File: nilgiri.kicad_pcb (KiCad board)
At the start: 2 copper layers, 130 x 72 mm, 32 parts, among them SW1 SW_PUSH, SW10 SW_PUSH, SW11 SW_PUSH, SW12 SW_PUSH, SW13 SW_PUSH, SW2 SW_PUSH, SW3 SW_PUSH, SW4 SW_PUSH, SW5 SW_PUSH, SW6 SW_PUSH, SW7 SW_PUSH, SW8 SW_PUSH, SW9 SW_PUSH, U1 ProMicro

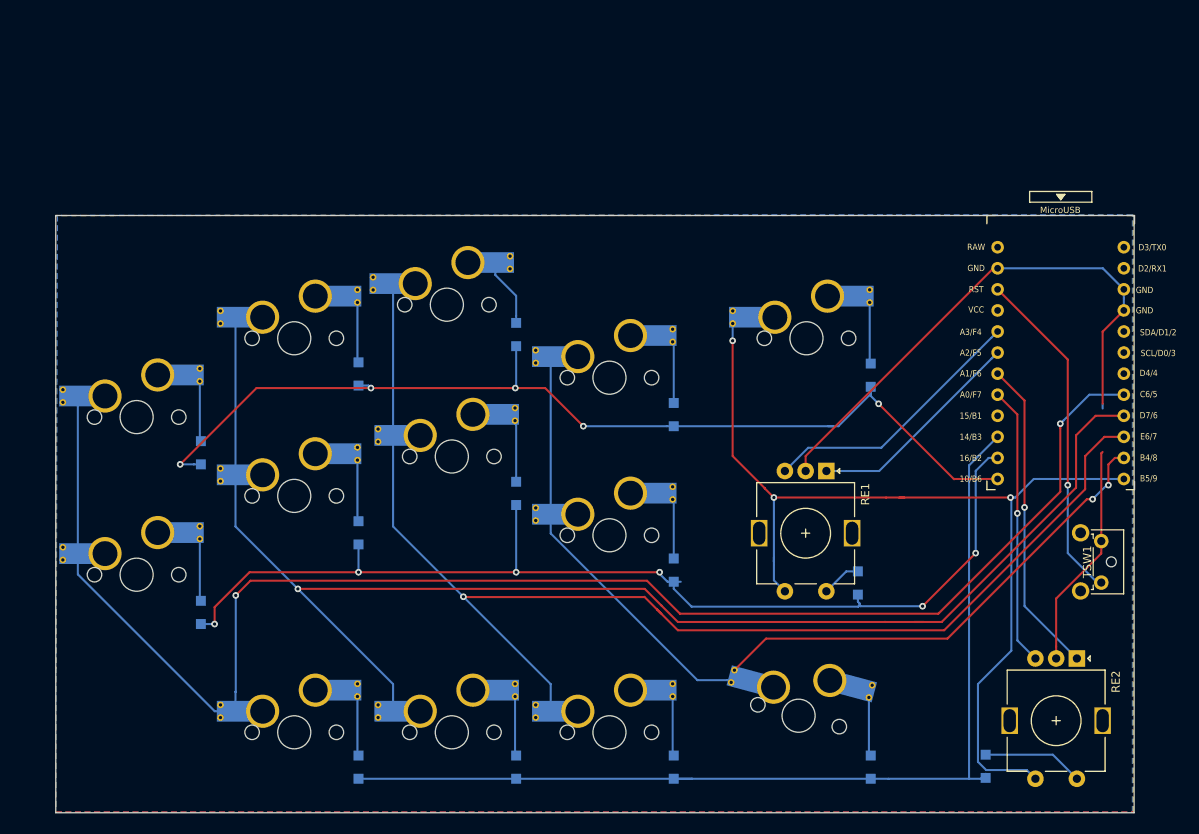
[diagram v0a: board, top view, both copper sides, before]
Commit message: merged onboard type / added footprints
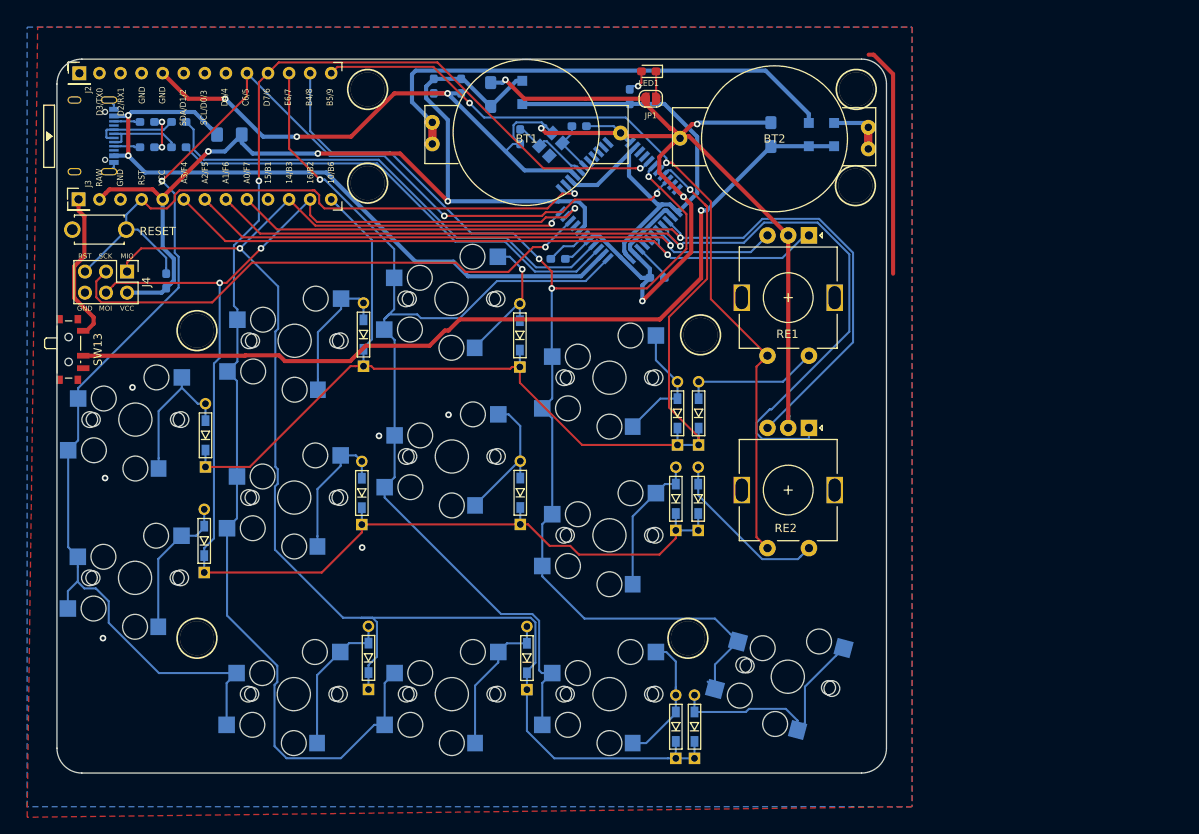
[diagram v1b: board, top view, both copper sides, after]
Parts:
- removed the D15 at (184.2, 76.2)
- removed D2: D, _keebio:D_SOD123F
- removed TSW1: SW_RESET, _keebio:SW_Tactile_SPST_Angled_MJTP1117
- added BT1: Battery_Cell, nilgiri:HU1632, F.Cu at (142.7, 47.0)
- added BT2: Battery_Cell, nilgiri:HU1632, F.Cu at (172.6, 47.8)
- added C1: 10u, Capacitor_Tantalum_SMD:CP_EIA-3216-10_Kemet-I_Pad1.58x1.35mm_HandSolder, B.Cu at (138.4, 42.4)
- added C2: 22p, Capacitor_SMD:C_0603_1608Metric_Pad1.05x0.95mm_HandSolder, B.Cu at (142.0, 47.5)
- added C3: 0.1u, Capacitor_SMD:C_0603_1608Metric_Pad1.05x0.95mm_HandSolder, B.Cu at (158.5, 64.5)
- added C5: 22p, Capacitor_SMD:C_0603_1608Metric_Pad1.05x0.95mm_HandSolder, B.Cu at (149.1, 46.2)
- added C6: 1u, Capacitor_SMD:C_0603_1608Metric_Pad1.05x0.95mm_HandSolder, B.Cu at (134.9, 41.4)
- added C7: 1u, Capacitor_SMD:C_0603_1608Metric_Pad1.05x0.95mm_HandSolder, B.Cu at (146.6, 62.2)
- added C8: 0.1u, Capacitor_SMD:C_0603_1608Metric_Pad1.05x0.95mm_HandSolder, B.Cu at (131.6, 41.4)
- added C9: 10u, Capacitor_Tantalum_SMD:CP_EIA-3216-10_Kemet-I_Pad1.58x1.35mm_HandSolder, B.Cu at (172.2, 47.2)
- added D21: 1N5819W, Keebio:D_SOD123F, B.Cu at (142.2, 42.2)
- added D31: 1N5819W, Keebio:D_SOD123F, B.Cu at (176.8, 47.2)
- added D32: 1N5819W, Keebio:D_SOD123F, B.Cu at (179.8, 47.2)
- added D5: 1N4148W, nilgiri:D3_TH_SMD, B.Cu at (103.9, 96.2)
- added F1: 500mA, Fuse:Fuse_1206_3216Metric_Pad1.42x1.75mm_HandSolder, B.Cu at (106.9, 47.2)
- added J1: USB-C, Connector_USB:USB_C_Receptacle_Palconn_UTC16-G, B.Cu at (90.5, 47.4)
- added J2: BAT-, Connector_PinHeader_2.54mm:PinHeader_1x01_P2.54mm_Vertical, F.Cu at (88.8, 39.9)
- added J3: BAT+, Connector_PinHeader_2.54mm:PinHeader_1x01_P2.54mm_Vertical, F.Cu at (88.8, 55.0)
- added J4: ISP, Connector_PinHeader_2.54mm:PinHeader_2x03_P2.54mm_Vertical, F.Cu at (94.6, 63.8)
- added JP1: LED_ENABLE, Jumper:SolderJumper-2_P1.3mm_Open_RoundedPad1.0x1.5mm, F.Cu at (157.7, 42.9)
- added LED1: PWR, LED_SMD:LED_0603_1608Metric_Pad1.05x0.95mm_HandSolder, F.Cu at (157.5, 39.6)
- added R1: 10k, Resistor_SMD:R_0603_1608Metric_Pad1.05x0.95mm_HandSolder, B.Cu at (99.3, 64.9)
- added R2: 1k, Resistor_SMD:R_0603_1608Metric_Pad1.05x0.95mm_HandSolder, B.Cu at (155.2, 42.7)
- added R3: 5.1k, Resistor_SMD:R_0603_1608Metric_Pad1.05x0.95mm_HandSolder, B.Cu at (97.0, 48.8)
- added R4: 5.1k, Resistor_SMD:R_0603_1608Metric_Pad1.05x0.95mm_HandSolder, B.Cu at (97.0, 45.7)
- added R5: 22, Resistor_SMD:R_0603_1608Metric_Pad1.05x0.95mm_HandSolder, B.Cu at (100.8, 48.8)
- added R6: 22, Resistor_SMD:R_0603_1608Metric_Pad1.05x0.95mm_HandSolder, B.Cu at (100.8, 45.7)
- added REF**: M2_spacer, nilgiri:M2_spacer, F.Cu at (162.2, 108.0)
- added REF**: M2_spacer, nilgiri:M2_spacer, F.Cu at (163.7, 71.4)
- added REF**: M2_spacer, nilgiri:M2_spacer, F.Cu at (103.0, 70.9)
- added REF**: M2_spacer, nilgiri:M2_spacer, F.Cu at (103.0, 108.0)
- added REF**: M2_spacer, nilgiri:M2_spacer, F.Cu at (123.6, 53.1)
- added REF**: M2_spacer, nilgiri:M2_spacer, F.Cu at (123.6, 41.8)
- added REF**: M2_spacer, nilgiri:M2_spacer, F.Cu at (182.5, 41.8)
- added REF**: M2_spacer, nilgiri:M2_spacer, F.Cu at (182.4, 53.4)
- added RST1: SW_RESET, kbd:ResetSW_1side, F.Cu at (91.2, 58.7)
- added U2: ProMicro, kbd:ProMicro_v3, F.Cu at (105.8, 47.5)
- added Y1: 16MHz, Crystal:Crystal_SMD_3225-4Pin_3.2x2.5mm, B.Cu at (145.7, 48.4)
- D10: renamed from D7; value D -> 1N4148W; footprint _keebio:D_SOD123F -> nilgiri:D3_TH_SMD
- D11: value D -> 1N4148W; footprint _keebio:D_SOD123F -> nilgiri:D3_TH_SMD
- D12: renamed from D8; value D -> 1N4148W; footprint _keebio:D_SOD123F -> nilgiri:D3_TH_SMD
- D13: renamed from D9; value D -> 1N4148W; footprint _keebio:D_SOD123F -> nilgiri:D3_TH_SMD
- D14: renamed from D10; value D -> 1N4148W; footprint _keebio:D_SOD123F -> nilgiri:D3_TH_SMD
- D15: renamed from D12; value D -> 1N4148W; footprint _keebio:D_SOD123F -> nilgiri:D3_TH_SMD
- D16: renamed from D13; value D -> 1N4148W; footprint _keebio:D_SOD123F -> nilgiri:D3_TH_SMD
- D17: renamed from D14; value D -> 1N4148W; footprint _keebio:D_SOD123F -> nilgiri:D3_TH_SMD
- D4: renamed from D1; value D -> 1N4148W; footprint _keebio:D_SOD123F -> nilgiri:D3_TH_SMD
- D6: renamed from D3; value D -> 1N4148W; footprint _keebio:D_SOD123F -> nilgiri:D3_TH_SMD
- D7: renamed from D4; value D -> 1N4148W; footprint _keebio:D_SOD123F -> nilgiri:D3_TH_SMD
- D8: renamed from D5; value D -> 1N4148W; footprint _keebio:D_SOD123F -> nilgiri:D3_TH_SMD
- D9: renamed from D6; value D -> 1N4148W; footprint _keebio:D_SOD123F -> nilgiri:D3_TH_SMD
- SW1, SW10, SW11, SW12, SW2, SW3, SW4, SW5, SW6, SW7, SW8, SW9: footprint KEYBOARD:CherryMX-Hotswap-v2 -> nilgiri:CherryMX_Choc_Hotswap
- SW13: value SW_PUSH -> SW_SPDT; footprint KEYBOARD:CherryMX-Hotswap-v2 -> Button_Switch_SMD:SW_SPDT_PCM12
- U1: value ProMicro -> ATmega32U4-AU; footprint KEYBOARD:ProMicro_v3.5 -> Keebio:ATMEGA32U4-AU; moved to B.Cu
- moved SW13 88.6 mm to (87.9, 73.2), turned to 270 degrees
- moved U1 56.9 mm to (153.9, 55.2), turned to 45 degrees
- moved D11 47.3 mm to (163.4, 91.2)
- moved RE2 42.6 mm to (176.8, 82.6)
- moved RE1 28.5 mm to (176.8, 59.4)
- moved D7 28.1 mm to (163.5, 80.8)
- moved D17 21.8 mm to (163.0, 118.6)
- moved D6 13.2 mm to (123.7, 110.3)
- moved D10 13.2 mm to (142.8, 110.3)
- moved D16 8.60 mm to (160.8, 91.2)
- moved D14 4.88 mm to (160.8, 118.6)
- moved SW12 4.88 mm to (174.2, 112.6)
- moved D9 4.82 mm to (122.9, 90.5)
- moved D8 4.79 mm to (123.1, 71.3)
- moved SW3 4.60 mm to (114.7, 114.7)
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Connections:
- D10 pad 1: Row2 -> MISO
- D11 pad 1: Row2 -> MOSI
- D13 pad 1: Row1 -> MOSI
- D14 pad 1: Row2 -> MISO
- D16 pad 1: Row1 -> MOSI
- D17 pad 1: Row2 -> MISO
- D6 pad 1: Row2 -> MISO
- D7 pad 1: Row1 -> Row0
- D9 pad 1: Row1 -> MOSI
- SW13 pad 1: Col4 -> Net-(J3-Pad1)
- U1 pad 1: (no net) -> Col2
- U1 pad 10: Col2 -> MOSI
- U1 pad 11: Col3 -> MISO
- U1 pad 12: Col4 -> Net-(U1-Pad12)
- U1 pad 13: Row0 -> RESET
- U1 pad 14: Row1 -> Net-(D21-Pad1)
- U1 pad 15: Row2 -> GND
- U1 pad 16: (no net) -> Net-(C2-Pad1)
- U1 pad 17: RB2 -> Net-(C5-Pad2)
- U1 pad 18: RA2 -> Net-(U1-Pad18)
- U1 pad 19: RA1 -> Net-(U1-Pad19)
- U1 pad 2: (no net) -> VBUS
- U1 pad 20: RB1 -> Net-(U1-Pad20)
- U1 pad 21: (no net) -> Net-(U1-Pad21)
- U1 pad 22: Reset -> Net-(U1-Pad22)
- U1 pad 24: (no net) -> Net-(D21-Pad1)
- U1 pad 3: GND -> D-
- U1 pad 4: GND -> D+
- U1 pad 5: (no net) -> GND
- U1 pad 6: (no net) -> Net-(C7-Pad1)
- U1 pad 7: (no net) -> RAW
- U1 pad 8: Col0 -> Net-(U1-Pad8)
- U1 pad 9: Col1 -> SCK
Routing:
- net MISO: track 0.00 -> 182.3 mm, vias 0 -> 2
- net MOSI: track 0.00 -> 175.6 mm, vias 0 -> 3
- net GND: track 93.2 -> 239.6 mm, vias 0 -> 16
- net Row1: track 129.7 -> 0.00 mm, vias 6 -> 0
- net Row2: track 120.7 -> 0.00 mm
- net RAW: track 0.00 -> 117.2 mm, vias 0 -> 3
- net Net-(C9-Pad1): track 10.7 -> 106.4 mm, vias 0 -> 1
- net VBUS: track 0.00 -> 84.8 mm, vias 0 -> 2
- net RA2: track 38.3 -> 117.8 mm
- net RESET: track 0.00 -> 77.3 mm, vias 0 -> 1
- net RB2: track 33.7 -> 105.6 mm
- net SCK: track 0.00 -> 66.1 mm, vias 0 -> 1
- net Net-(D21-Pad1): track 0.00 -> 62.0 mm
- net Net-(BT1-Pad1): track 0.00 -> 60.7 mm
- net D+: track 0.00 -> 59.0 mm
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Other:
- board size 130 x 72 mm -> 100 x 86.1 mm
- rule trace_min: 0.2 -> 0.1
- board text added: "GND"
- board text added: "MIO"
- board text added: "MOI"
- board text added: "RST"
- board text added: "SCK"
- board text added: "VCC"
- board text added: "are not correct, except key switches."
- board text added: "note: the positions or sizes"
- board text added: "shaft:7mm"

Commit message: combined Onboard type and Pro Micro type
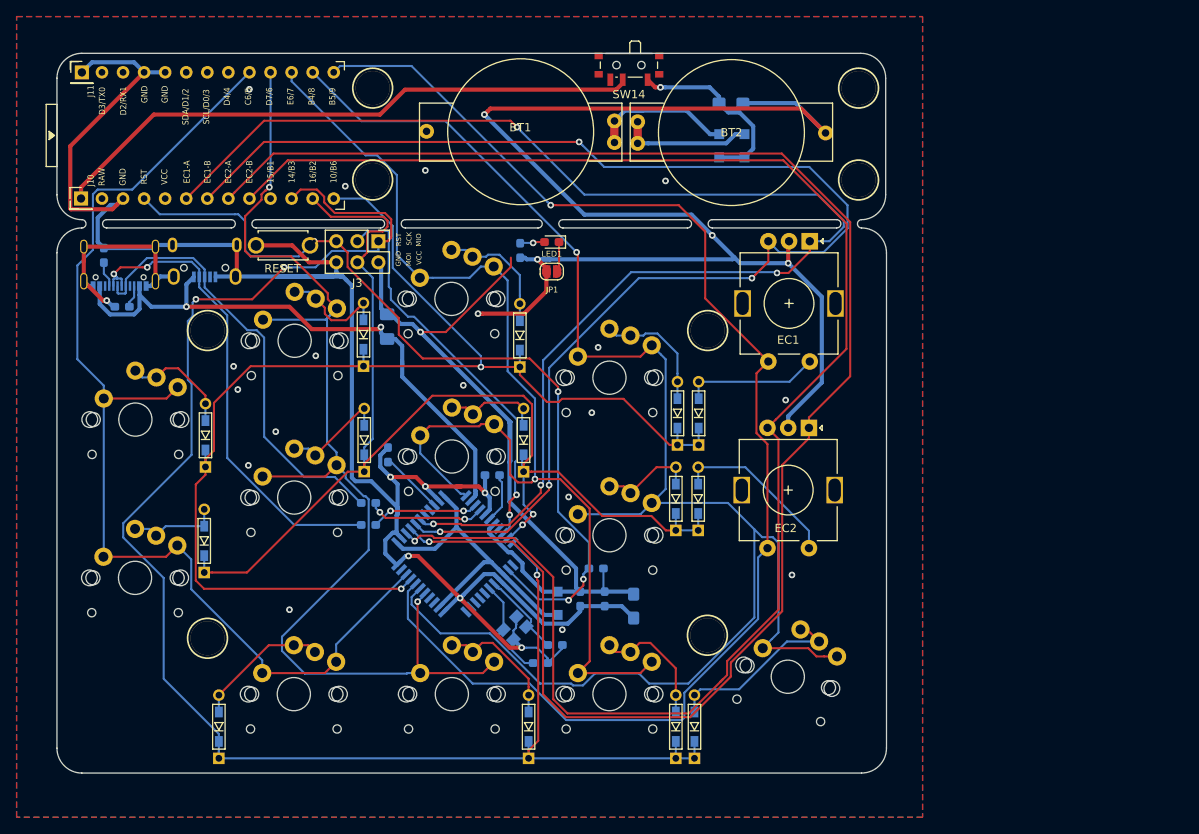
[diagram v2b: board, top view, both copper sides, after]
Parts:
- removed the C5 at (149.1, 46.2)
- removed C9: 10u, Capacitor_Tantalum_SMD:CP_EIA-3216-10_Kemet-I_Pad1.58x1.35mm_HandSolder
- removed the D5 at (103.9, 96.2)
- removed the D8 at (123.1, 71.3)
- removed J4: ISP, Connector_PinHeader_2.54mm:PinHeader_2x03_P2.54mm_Vertical
- removed the R3 at (97.0, 48.8)
- removed REF** (x8): M2_spacer, nilgiri:M2_spacer
- added C10: 10u, Capacitor_Tantalum_SMD:CP_EIA-3216-10_Kemet-I_Pad1.58x1.35mm_HandSolder, B.Cu at (167.4, 43.5)
- added C3: 1u, Capacitor_SMD:C_0603_1608Metric_Pad1.05x0.95mm_HandSolder, B.Cu at (138.6, 88.3)
- added D2: 1N4148W, nilgiri:D3_TH_SMD, B.Cu at (103.9, 96.2)
- added D4: 1N4148W, nilgiri:D3_TH_SMD, B.Cu at (123.1, 71.3)
- added H1: MountingHole, nilgiri:M2_spacer, F.Cu at (124.2, 41.6)
- added H2: MountingHole, nilgiri:M2_spacer, F.Cu at (124.2, 52.7)
- added H3: MountingHole, nilgiri:M2_spacer, F.Cu at (182.8, 41.6)
- added H4: MountingHole, nilgiri:M2_spacer, F.Cu at (182.8, 52.7)
- added H5: MountingHole, nilgiri:M2_spacer, F.Cu at (104.3, 70.9)
- added H6: MountingHole, nilgiri:M2_spacer, F.Cu at (104.3, 108.0)
- added H7: MountingHole, nilgiri:M2_spacer, F.Cu at (164.6, 70.9)
- added H8: MountingHole, nilgiri:M2_spacer, F.Cu at (164.6, 107.6)
- added J10: BAT+, Connector_PinHeader_2.54mm:PinHeader_1x01_P2.54mm_Vertical, F.Cu at (89.0, 55.0)
- added J11: BAT-, Connector_PinHeader_2.54mm:PinHeader_1x01_P2.54mm_Vertical, F.Cu at (89.2, 39.8)
- added R5: 1k, Resistor_SMD:R_0603_1608Metric_Pad1.05x0.95mm_HandSolder, B.Cu at (142.0, 61.2)
- BT1, BT2: value Battery_Cell -> 3V
- C7: value 1u -> 22p
- D21, D31, D32: value 1N5819W -> MBR120
- J2: value BAT- -> USB_B_Micro; footprint Connector_PinHeader_2.54mm:PinHeader_1x01_P2.54mm_Vertical -> Connector_USB:USB_Micro-B_Wuerth_629105150521; moved to B.Cu
- J3: value BAT+ -> ISP; footprint Connector_PinHeader_2.54mm:PinHeader_1x01_P2.54mm_Vertical -> Connector_PinHeader_2.54mm:PinHeader_2x03_P2.54mm_Vertical
- R1: value 10k -> 5.1k
- R2: value 1k -> 5.1k
- R4: value 5.1k -> 22
- R6: value 22 -> 10k
- SW1, SW10, SW11, SW12, SW2, SW3, SW4, SW5, SW6, SW7, SW8, SW9: footprint nilgiri:CherryMX_Choc_Hotswap -> kbd:CherryMX_Choc_1u
- SW14: renamed from SW13; value SW_SPDT -> PWR
- moved SW14 75.3 mm to (155.1, 39.2), turned to 180 degrees
- moved R6 73.7 mm to (151.2, 99.5)
- moved R2 66.2 mm to (94.0, 68.0), turned to 0 degrees
- moved C4 64.3 mm to (149.2, 103.2)
- moved C2 64.2 mm to (152.2, 103.2)
- moved C1 64.0 mm to (155.7, 104.1), turned to 270 degrees
- moved D21 61.7 mm to (146.5, 103.8)
- moved C6 61.4 mm to (146.2, 108.8), turned to 0 degrees
- moved Y1 58.5 mm to (141.3, 106.8), turned to 45 degrees
- moved R4 55.4 mm to (123.7, 94.3)
- moved C7 48.8 mm to (144.4, 111.0), turned to 180 degrees
- moved R3 48.6 mm to (123.7, 91.7)
- moved U1 47.0 mm to (134.1, 97.8), turned to 225 degrees
- moved C5 38.8 mm to (126.0, 85.8), turned to 90 degrees
- moved J3 36.5 mm to (124.9, 60.1), turned to 270 degrees
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- renumbered C6 to C2, C8 to C4, C3 to C5, C2 to C6, D4 to D1, D15 to D10, D16 to D11, D17 to D12, D7 to D13, D11 to D14, D6 to D3, D9 to D5, D10 to D6, D12 to D7, D13 to D8, D14 to D9, RE1 to EC1, RE2 to EC2, R5 to R3, RST1 to SW13
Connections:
- C1 pad 1: RAW -> VCC
- C2 pad 1: RAW -> VCC
- C4 pad 1: RAW -> VCC
- C7 pad 1: Net-(C7-Pad1) -> GND
- C7 pad 2: GND -> Net-(C7-Pad2)
- D21 pad 2: RAW -> VCC
- D31 pad 1: Net-(C9-Pad1) -> Net-(C10-Pad1)
- D32 pad 1: Net-(C9-Pad1) -> Net-(C10-Pad1)
- F1 pad 1: RAW -> VCC
- F1 pad 2: VBUS -> RAW
- J1 pad A4: VBUS -> RAW
- J1 pad A6: Net-(J1-PadA6) -> D+
- J1 pad A7: Net-(J1-PadA7) -> D-
- J1 pad A9: VBUS -> RAW
- J1 pad B4: VBUS -> RAW
- J1 pad B6: Net-(J1-PadA6) -> D+
- J1 pad B7: Net-(J1-PadA7) -> D-
- J1 pad B9: VBUS -> RAW
- J2 pad 1: GND -> RAW
- J3 pad 1: Net-(J3-Pad1) -> MISO
- JP1 pad 1: Net-(JP1-Pad1) -> GND
- JP1 pad 2: GND -> Net-(JP1-Pad2)
- LED1 pad 1: Net-(JP1-Pad1) -> Net-(JP1-Pad2)
- R1 pad 1: RAW -> GND
- R1 pad 2: RESET -> Net-(J1-PadA5)
- R2 pad 1: Net-(D21-Pad1) -> GND
- R2 pad 2: Net-(LED1-Pad2) -> Net-(J1-PadB5)
- R3 pad 1: D- -> Net-(R3-Pad1)
- R3 pad 2: Net-(J1-PadA7) -> D+
- R4 pad 1: GND -> Net-(R4-Pad1)
- R4 pad 2: Net-(J1-PadB5) -> D-
- R6 pad 1: D+ -> VCC
- R6 pad 2: Net-(J1-PadA6) -> RESET
- SW14 pad 1: Net-(J3-Pad1) -> Net-(C10-Pad1)
- SW14 pad 2: Net-(C9-Pad1) -> Net-(J10-Pad1)
- U1 pad 17: Net-(C5-Pad2) -> Net-(C7-Pad2)
- U1 pad 2: VBUS -> RAW
- U1 pad 3: D- -> Net-(R4-Pad1)
- U1 pad 4: D+ -> Net-(R3-Pad1)
- U1 pad 6: Net-(C7-Pad1) -> Net-(C3-Pad1)
- U1 pad 7: RAW -> VCC
- U2 pad 21: RAW -> Net-(U2-Pad21)
- U2 pad 24: RAW -> Net-(U2-Pad24)
- Y1 pad 1: Net-(C5-Pad2) -> Net-(C7-Pad2)
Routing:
- net GND: track 239.6 -> 425.0 mm, vias 16 -> 28
- net Net-(C9-Pad1): track 106.4 -> 0.00 mm, vias 1 -> 0
- net VCC: track 0.00 -> 96.6 mm, vias 0 -> 1
- net RB2: track 105.6 -> 197.8 mm
- net RB1: track 73.9 -> 164.7 mm, vias 1 -> 4
- net VBUS: track 84.8 -> 0.00 mm, vias 2 -> 0
- net RA1: track 82.5 -> 165.2 mm, vias 1 -> 4
- net RA2: track 117.8 -> 200.0 mm
- net Net-(J10-Pad1): track 0.00 -> 72.3 mm
- net Col4: track 100.9 -> 163.5 mm, vias 2 -> 1
- net Col3: track 146.7 -> 195.9 mm, vias 3 -> 1
- net RAW: track 117.2 -> 72.3 mm, vias 3 -> 2
- net Net-(BT1-Pad1): track 60.7 -> 18.3 mm
- net Col0: track 168.6 -> 132.9 mm, vias 3 -> 0
- net MOSI: track 175.6 -> 144.9 mm, vias 3 -> 2
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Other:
- board size 100 x 86.1 mm -> 100 x 86.8 mm

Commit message: 全体調整
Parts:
- added H99: LOGO, nilgiri:nil_logo, F.Cu at (94.6, 119.0)
- EC1, EC2: value Rotary_Encoder_Switch -> EC11E18244A5
- H1, H2, H3, H4: footprint nilgiri:M2_spacer -> nilgiri:M2_vis
- J1, J2: moved to F.Cu
- J10, J11: footprint Connector_PinHeader_2.54mm:PinHeader_1x01_P2.54mm_Vertical -> nilgiri:Hole 0.8mm
- moved J3 31.6 mm to (156.5, 61.1)
- moved J2 14.6 mm to (89.9, 66.6), turned to 270 degrees
- moved R1 8.10 mm to (99.9, 61.5)
- moved F1 7.99 mm to (130.7, 76.8), turned to 180 degrees
- moved R2 7.19 mm to (97.2, 61.5), turned to 270 degrees
- moved SW13 5.10 mm to (108.3, 60.3), turned to 0 degrees
- moved J1 4.90 mm to (98.6, 62.9), turned to 180 degrees
- moved H8 3.71 mm to (164.4, 111.3)
- moved H6 3.63 mm to (102.9, 111.3)
- moved BT1 3.00 mm to (139.0, 47.0)
- moved R4 2.65 mm to (123.7, 91.7)
- moved R3 2.58 mm to (123.8, 94.2)
- moved SW14 2.00 mm to (153.1, 39.2)
- moved H5 1.43 mm to (102.9, 70.9)
- moved H4 1.04 mm to (181.8, 53.0)
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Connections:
- J1 pad A8: Net-(J1-PadA8) -> (no net)
- J1 pad B8: Net-(J1-PadB8) -> (no net)
- J2 pad 4: Net-(J2-Pad4) -> (no net)
- SW14 pad 3: Net-(SW14-Pad3) -> (no net)
- U1 pad 12: Net-(U1-Pad12) -> (no net)
- U1 pad 18: Net-(U1-Pad18) -> (no net)
- U1 pad 19: Net-(U1-Pad19) -> (no net)
- U1 pad 20: Net-(U1-Pad20) -> (no net)
- U1 pad 21: Net-(U1-Pad21) -> (no net)
- U1 pad 22: Net-(U1-Pad22) -> (no net)
- U1 pad 25: Net-(U1-Pad25) -> (no net)
- U1 pad 26: Net-(U1-Pad26) -> (no net)
- U1 pad 32: Net-(U1-Pad32) -> (no net)
- U1 pad 40: Net-(U1-Pad40) -> (no net)
- U1 pad 41: Net-(U1-Pad41) -> (no net)
- U1 pad 8: Net-(U1-Pad8) -> (no net)
- U2 pad 1: Net-(U2-Pad1) -> (no net)
- U2 pad 16: Net-(U2-Pad16) -> (no net)
- U2 pad 2: Net-(U2-Pad2) -> (no net)
- U2 pad 21: Net-(U2-Pad21) -> (no net)
- U2 pad 24: Net-(U2-Pad24) -> (no net)
- U2 pad 5: Net-(U2-Pad5) -> (no net)
- U2 pad 6: Net-(U2-Pad6) -> (no net)
- U2 pad 7: Net-(U2-Pad7) -> (no net)
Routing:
- net MISO: track 200.1 -> 241.5 mm, vias 3 -> 2
- net MOSI: track 144.9 -> 185.4 mm
- net RESET: track 102.9 -> 131.0 mm, vias 4 -> 3
- net GND: track 425.0 -> 440.5 mm, vias 28 -> 33
- net Col3: track 195.9 -> 185.5 mm
- net D+: track 53.5 -> 63.3 mm, vias 0 -> 3
- net SCK: track 48.4 -> 41.0 mm, vias 2 -> 3
- net RAW: track 72.3 -> 65.9 mm, vias 2 -> 3
- net VCC: track 96.6 -> 102.7 mm, vias 1 -> 0
- net RA1: track 165.2 -> 170.6 mm
- net Row0: track 154.3 -> 150.4 mm
- net D-: track 58.3 -> 54.7 mm, vias 2 -> 4
- net Net-(C10-Pad1): track 22.8 -> 26.2 mm
- net Col0: track 132.9 -> 130.2 mm
- net Col1: track 141.9 -> 139.5 mm
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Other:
- board text added: "*FOR BLE MICRO PRO*"
- board text added: "Keypad for Artists"
- board text added: "v0.32(191029)"
